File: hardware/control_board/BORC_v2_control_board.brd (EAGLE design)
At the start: 75 x 74.8 mm, 170 parts, among them J1 USB Female Type C Connector, J2 QWIIC_RIGHT_ANGLE, J3 M20-8900405, J5 S2B-XH-A(LF)(SN), Q1 SSM3J374R,LF, Q10 BSS138PW,115, Q11 SSM3J374R,LF, Q16 UMT3904T106, Q2 SSM3J374R,LF, Q3 BSS138PW,115, Q4 UMT3904T106, Q5 SSM3J374R,LF, Q6 UMT3904T106, Q7 SSM3J374R,LF, Q9 BSS138PW,115, SW1 SPST_TACT-KMR2, U1 ATMEGA1284P-MU, U11 INA219AIDCNR, U2 SHT40-BD1B, U3 PCA9685, U4 MCP1703CB, U5 POLOLU_STEPUP_U3V40F5, U6 915MHz, U7 AT25F512BJEDEC_3.9MM, U8 FT231XQ-R, U9 MCP73833T-AMI/MF, Y1 16 MHz

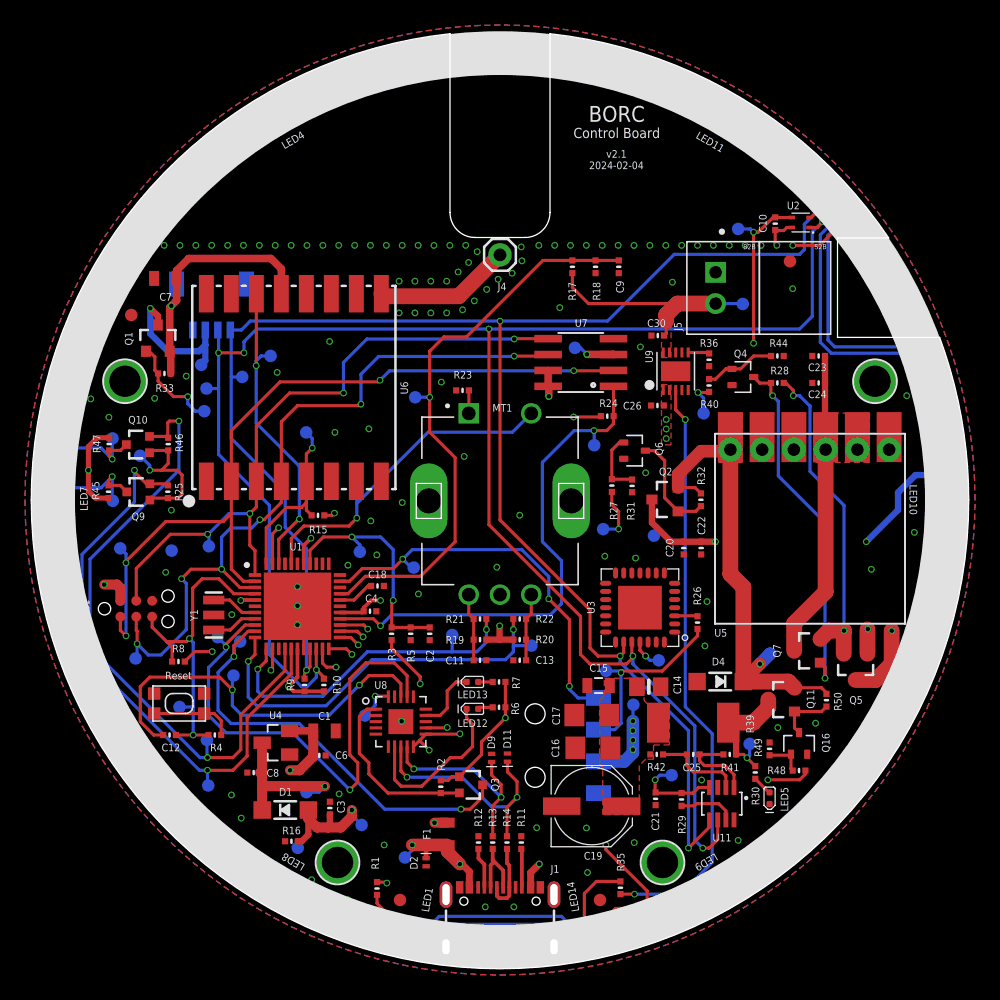
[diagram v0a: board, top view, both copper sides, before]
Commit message: v2.2 - bug fixes
- Fixed display power circuit with PNP (active low)
- Replace charger with MCP73781 (can toggle between 500mA and 1000mA with jumper)
- Fixed battery JST with PH connector
- Fixed 5V switch to switch before 5V boost instead of after to avoid voltage drop
- Merged 5V power with LED power
- Connected USB shield to ground
- Connected rotary encoder shield to ground
- Removed blue LED from 5V power to avoid voltage drop
- Thickened some power traces where needed
- Minor adjustments to traces, component placement and silkscreen to accommodate design changes
- Thickened mounting holes
- Added visible ground silkscreen for servo
- Renamed LEDs to match dotstar in code
- Better info in schematics where needed
- Updated dimensions, schematics, gerber, renders, BOM, 3D step files
- ERC/DRC done
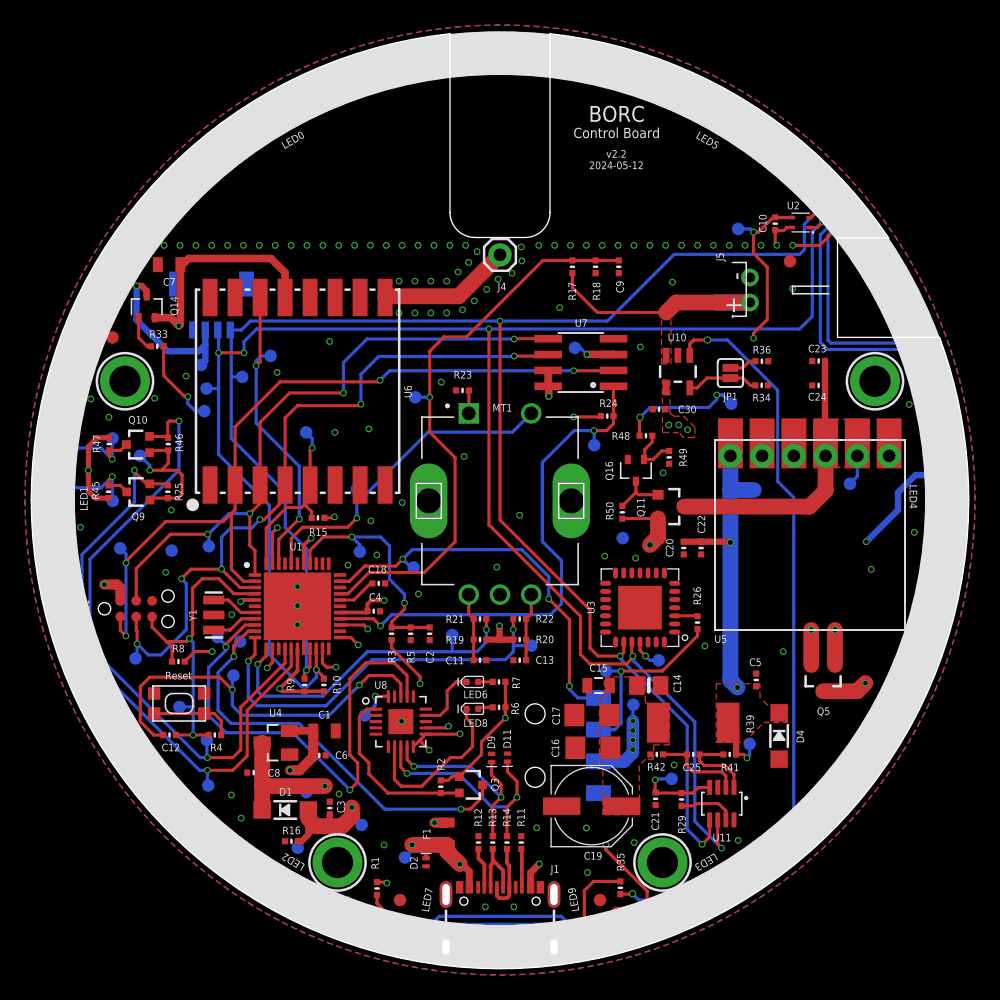
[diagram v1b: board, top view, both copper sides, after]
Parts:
- removed C26: 0.1uF, Adafruit Feather 32u4 Bluefruit LE:MICROBUILDER__0402MP
- removed LED10, LED11: APA102, microbuilder:APA102_2020
- removed LED12: GREEN, Seeed-LED:LED-0402
- removed LED14: YELLOW, Seeed-LED:LED-0402
- removed MH1, U$3, U$4, U$7: MOUNTINGHOLE2.5, ADS1x15:MOUNTINGHOLE_2.5_PLATED
- removed Q1, Q2, Q7: SSM3J374R,LF, MOSFETs:SOT23-3
- removed Q4, Q6: UMT3904T106, SOT65P210X100-3N:SOT65P210X100-3N
- removed R27, R40: 1K, Adafruit Feather 32u4 Bluefruit LE:MICROBUILDER__0402MP
- removed R28, R30, R31, R32, R44: 10K, Adafruit Feather 32u4 Bluefruit LE:MICROBUILDER__0402MP
- removed TP3: RX, Adafruit Feather 32u4 Bluefruit LE:MICROBUILDER_TESTPOINT_ROUND_1MM
- removed U9: MCP73833T-AMI/MF, microbuilder:DFN10_3X3MM
- added C5: 0.1uF, Adafruit Feather 32u4 Bluefruit LE:MICROBUILDER__0402MP
- added JP1: JUMPER-SMT_2_NC_PASTE_SILK, SparkFun-Jumpers:SMT-JUMPER_2_NC_PASTE_SILK
- added LED0, LED2, LED3: APA102, microbuilder:APA102_2020
- added Q14: UMT3906T106, UMT390X:SOT65P210X100-3N-PNP
- added R34: 2K, Adafruit Feather 32u4 Bluefruit LE:MICROBUILDER__0402MP
- added TP22: RAW_PWR, Adafruit Feather 32u4 Bluefruit LE:MICROBUILDER_TESTPOINT_ROUND_1MM
- added U$10, U$11, U$8, U$9: MICROBUILDER_MOUNTINGHOLE2.5_THICK, Adafruit Feather 32u4 Bluefruit LE:MICROBUILDER_MOUNTINGHOLE_2.5_PLATED_THICK
- added U10: MCP73831, SparkFun:SOT23-5
- J5: value S2B-XH-A(LF)(SN) -> (none); device S2B-XH-A_LF__SN_:JST_S2B-XH-A(LF)(SN) -> adafruit:JST-PH-2-THM-RA
- LED1: value RED -> APA102; device Seeed-LED:LED-0402 -> microbuilder:APA102_2020
- LED5: value BLUE -> APA102; device Seeed-LED:LED-0402 -> microbuilder:APA102_2020
- LED7: value APA102 -> RED; device microbuilder:APA102_2020 -> Seeed-LED:LED-0402
- LED8: value APA102 -> GREEN; device microbuilder:APA102_2020 -> Seeed-LED:LED-0402
- LED9: value APA102 -> YELLOW; device microbuilder:APA102_2020 -> Seeed-LED:LED-0402
- R33: value 10K -> 1K
- R36: value 1K -> 2K
- TP24: value RX -> 5V_POWER
- moved LED4 62.1 mm to (73.3, 37.5), turned to 270 degrees
- moved LED5 54.9 mm to (55.6, 68.5), turned to 330 degrees
- moved LED1 46.0 mm to (1.67, 37.5), turned to 90 degrees
- moved LED7 46.0 mm to (30.2, 1.45), turned to 350 degrees
- moved R48 29.5 mm to (49.2, 42.6), turned to 180 degrees
- moved Q16 25.4 mm to (48.4, 39.9), turned to 270 degrees
- moved R49 24.7 mm to (51.0, 40.9), turned to 270 degrees
- moved R50 22.2 mm to (47.3, 36.5), turned to 90 degrees
- moved LED8 21.2 mm to (35.3, 20.8), turned to 180 degrees
- moved Q11 17.8 mm to (51.1, 37.0), turned to 270 degrees
- moved TP25 13.2 mm to (57.8, 38.3), turned to 0 degrees
- moved LED9 11.8 mm to (44.7, 1.47), turned to 190 degrees
- moved D4 6.41 mm to (59.8, 18.6), turned to 270 degrees
- moved C30 5.90 mm to (50.2, 44.8)
- moved R36 4.22 mm to (58.5, 48.6), turned to 180 degrees
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- renumbered LED13 to LED6
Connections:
- removed net LED_5V: C20.1, C22.1, LED10.3, LED11.3, LED4.3, LED7.3, LED8.3, LED9.3, Q2.3, R45.1, R47.1
- removed net LED_POWER: R27.2, TP3.P$1, U1.24
- removed net N$18: Q2.1, Q6.3, R32.2
- removed net N$20: Q6.1, R27.1, R31.1
- removed net N$27: R36.2, U9.P$6
- removed net N$31: Q4.3, Q7.1, R28.2
- removed net N$34: Q4.1, R40.1, R44.1
- removed net N$46: LED5.+, R30.2
- removed net PWR_IN: C23.1, C24.1, Q7.3, U5.P$2, U5.P$3, U5.VIN@1, U5.VIN@2
- removed net SERVO_POWER: R48.2, U1.22
- removed net SERVO_RAW: Q11.3, R30.1, R39.2, R41.1, TP30.P$1
- new net N$19: Q14.2, R33.1
- new net N$21: JP1.2, R34.2, U10.5
- new net N$22: JP1.1, R36.2
- new net RAW_PWR: C23.1, C24.1, Q11.3, TP22.P$1, U5.P$2, U5.P$3, U5.VIN@1, U5.VIN@2
- net 5V: now also C20.1, C22.1, C5.1, LED0.3, LED1.3, LED2.3, LED3.3, LED4.3, LED5.3, R39.2, R41.1, R45.1, R47.1, TP30.P$1; no longer Q11.2, Q2.2, R32.1, R50.1
- net 5V_POWER: now also R48.2; no longer R40.2
- net C2: now also LED0.2, LED1.5; no longer LED4.2, LED7.5
- net C3: now also LED1.2, LED2.5; no longer LED7.2, LED8.5
- net C4: now also LED2.2, LED3.5; no longer LED8.2, LED9.5
- net C5: now also LED3.2, LED4.5; no longer LED10.5, LED9.2
- net C6: now also LED4.2, LED5.5; no longer LED10.2, LED11.5
- net D2: now also LED0.1, LED1.6; no longer LED4.1, LED7.6
- net D3: now also LED1.1, LED2.6; no longer LED7.1, LED8.6
- net D4: now also LED2.1, LED3.6; no longer LED8.1, LED9.6
- net D5: now also LED3.1, LED4.6; no longer LED10.6, LED9.1
- net D6: now also LED4.1, LED5.6; no longer LED10.1, LED11.6
- net DISPLAY_3V3: now also Q14.3; no longer Q1.3
- net DISPLAY_POWER: no longer Q1.1
- net GND: now also C5.2, J1.SHLD1, J1.SHLD2, J1.SHLD3, J1.SHLD4, J5.2, LED0.4, LED1.4, LED2.4, LED3.4, LED5.4, LED7.-, MT1.S1, MT1.S2, R34.1, U10.2; no longer C26.1, J5.1, LED1.-, LED10.4, LED11.4, LED5.-, LED7.4, LED8.4, LED9.4, Q4.2, Q6.2, R31.2, R44.2, U9.P$5
- net LED_CLK_5V: now also LED0.5; no longer LED4.5
- net LED_DATA_5V: now also LED0.6; no longer LED4.6
- net N$10: now also LED8.-; no longer LED12.-
- net N$16: now also LED9.-; no longer LED14.-
- net N$2: now also LED7.+; no longer LED1.+
- net N$6: now also LED8.+; no longer LED12.+
- net N$9: now also U10.1; no longer U9.P$3
- net VBAT: now also J5.1, U10.3; no longer C30.1, J5.2, U9.P$10, U9.P$9
- net VBUS_FUSED: now also C30.1, LED9.+, U10.4; no longer C26.2, LED14.+, U9.P$1, U9.P$2
- net VCC: now also Q14.1; no longer Q1.2, R33.1
- net VIN: now also Q11.2, R50.1; no longer Q7.2, R28.1
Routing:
- net LED_5V: track 249.5 -> 0.00 mm, vias 9 -> 0
- net 5V: track 38.2 -> 270.1 mm, vias 1 -> 11
- net SERVO_POWER: track 42.9 -> 0.00 mm, vias 2 -> 0
- net LED_POWER: track 35.0 -> 0.00 mm, vias 2 -> 0
- net N$31: track 28.4 -> 0.00 mm, vias 2 -> 0
- net RAW_PWR: track 0.00 -> 24.7 mm
- net PWR_IN: track 24.7 -> 0.00 mm
- net N$9: track 47.4 -> 61.0 mm
- net SERVO_RAW: track 10.3 -> 0.00 mm, vias 1 -> 0
- net 5V_POWER: track 63.7 -> 72.4 mm, vias 2 -> 3
- net N$18: track 8.36 -> 0.00 mm
- net N$21: track 0.00 -> 5.81 mm
- net N$34: track 5.72 -> 0.00 mm
- net N$20: track 5.16 -> 0.00 mm
- net VIN: track 94.1 -> 90.0 mm
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- added copper zone on layer 1, net RAW_PWR
- removed copper zone on layer 1, net PWR_IN
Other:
- board text added: "v2.2 2024-05-12"
- board text removed: "v2.1 2024-02-04"
